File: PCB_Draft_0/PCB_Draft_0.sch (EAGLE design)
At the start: 7 parts, among them IC1 ADS7828, IC2 PCA9534PW

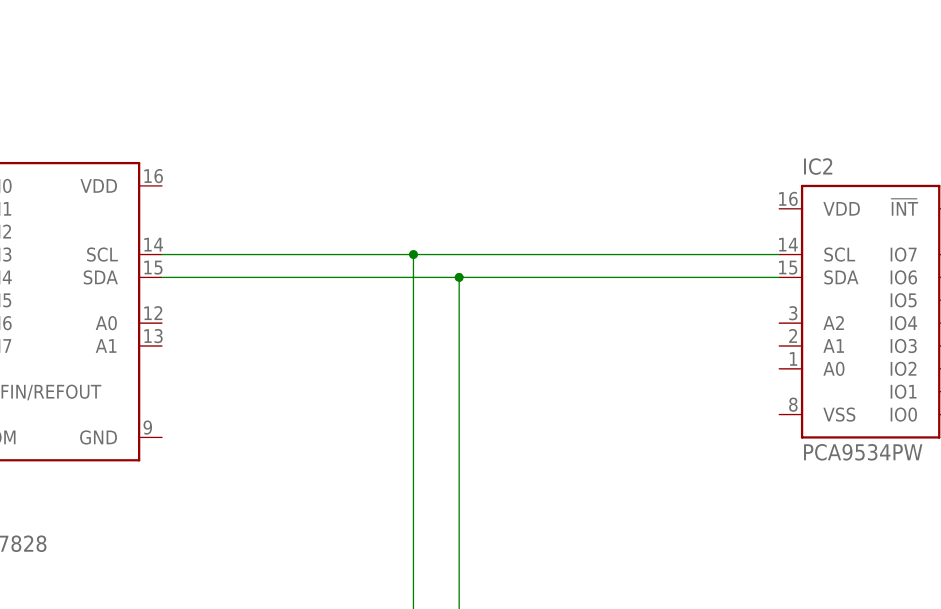
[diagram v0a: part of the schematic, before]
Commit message: With connected 3V and GND pins this time
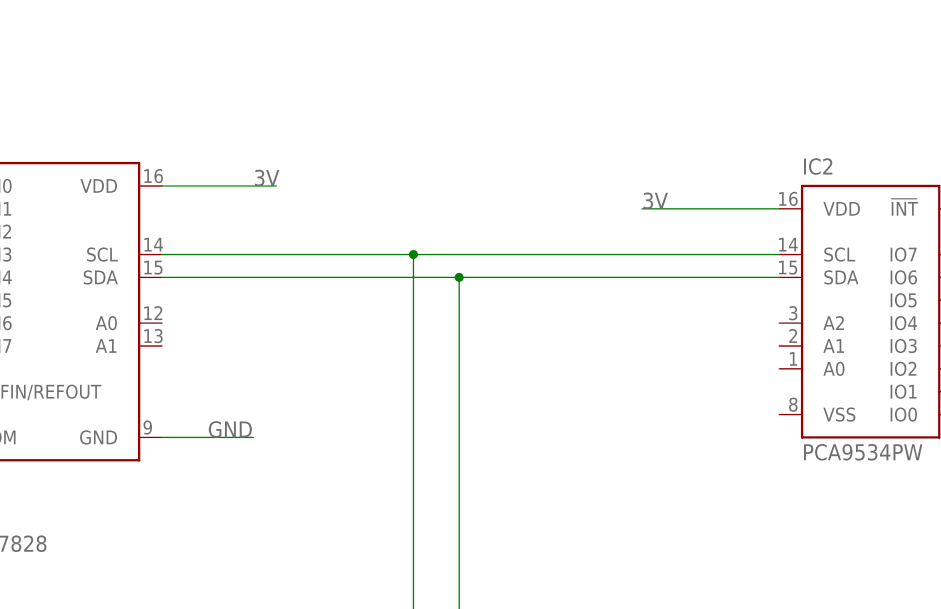
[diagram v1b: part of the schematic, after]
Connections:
- net 3V: now also IC1.VDD, IC2.VDD
- net GND: now also IC1.GND
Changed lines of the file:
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@@
 <label x="17.78" y="99.06" size="1.778" layer="95"/>
+</segment>
+<segment>
+<pinref part="IC1" gate="G$1" pin="VDD"/>
+<wire x1="104.14" y1="154.94" x2="116.84" y2="154.94" width="0.1524" layer="91"/>
+<label x="114.3" y="154.94" size="1.778" layer="95"/>
+</segment>
+<segment>
+<pinref part="IC2" gate="P" pin="VDD"/>
+<wire x1="172.72" y1="152.4" x2="157.48" y2="152.4" width="0.1524" layer="91"/>
+<label x="157.48" y="152.4" size="1.778" layer="95"/>
 </segment>
 </net>
@@
 <label x="17.78" y="91.44" size="1.778" layer="95"/>
 </segment>
+<segment>
+<pinref part="IC1" gate="G$1" pin="GND"/>
+<wire x1="104.14" y1="127" x2="114.3" y2="127" width="0.1524" layer="91"/>
+<label x="109.22" y="127" size="1.778" layer="95"/>
+</segment>
 </net>

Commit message: Added I2C Headers
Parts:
- added 3V, GND, SCL, SDA: (no value), con-lsta:FE06-1
- renumbered IC1 to ADC_X, IC2 to GPIO_X
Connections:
- net 3V: now also 3V.1, 3V.2, 3V.3, 3V.4, 3V.5, 3V.6
- net GND: now also GND.1, GND.2, GND.3, GND.4, GND.5, GND.6
- net SCL: now also SCL.1, SCL.2, SCL.3, SCL.4, SCL.5, SCL.6
- net SDA: now also SDA.1, SDA.2, SDA.3, SDA.4, SDA.5, SDA.6
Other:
- moved on the sheet: R1, R2

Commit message: SomeStuff
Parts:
- removed 3V, GND, SCL, SDA: (no value), con-lsta:FE06-1
- added A_COM: (no value), ME507:SCREWTERM_3P_254
- added C1: 5u, rcl:C-USC0805
- added I2C: (no value), con-lstb:MA04-1
- added R3: 0, rcl:R-US_M0805
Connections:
- new net A_COM: ADC_X.COM, A_COM-3.1, C1.2, R3.1
- new net INT: GPIO_X.!INT, MS1.GPIO5
- new net N$17: ADC_X.REFIN/REFOUT, C1.1
- net 3V: now also A_COM-1.1, I2C.1; no longer 3V.1, 3V.2, 3V.3, 3V.4, 3V.5, 3V.6
- net GND: now also ADC_X.A0, ADC_X.A1, A_COM-2.1, GPIO_X.A0, GPIO_X.A1, GPIO_X.A2, GPIO_X.VSS, I2C.4, R3.2; no longer GND.1, GND.2, GND.3, GND.4, GND.5, GND.6
- net SCL: now also I2C.3; no longer SCL.1, SCL.2, SCL.3, SCL.4, SCL.5, SCL.6
- net SDA: now also I2C.2; no longer SDA.1, SDA.2, SDA.3, SDA.4, SDA.5, SDA.6
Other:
- moved on the sheet: A-1, A-2, A-3, A-4, A-5, A-6, A-7, A-8, ADC_X, D-1, D-2, D-3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

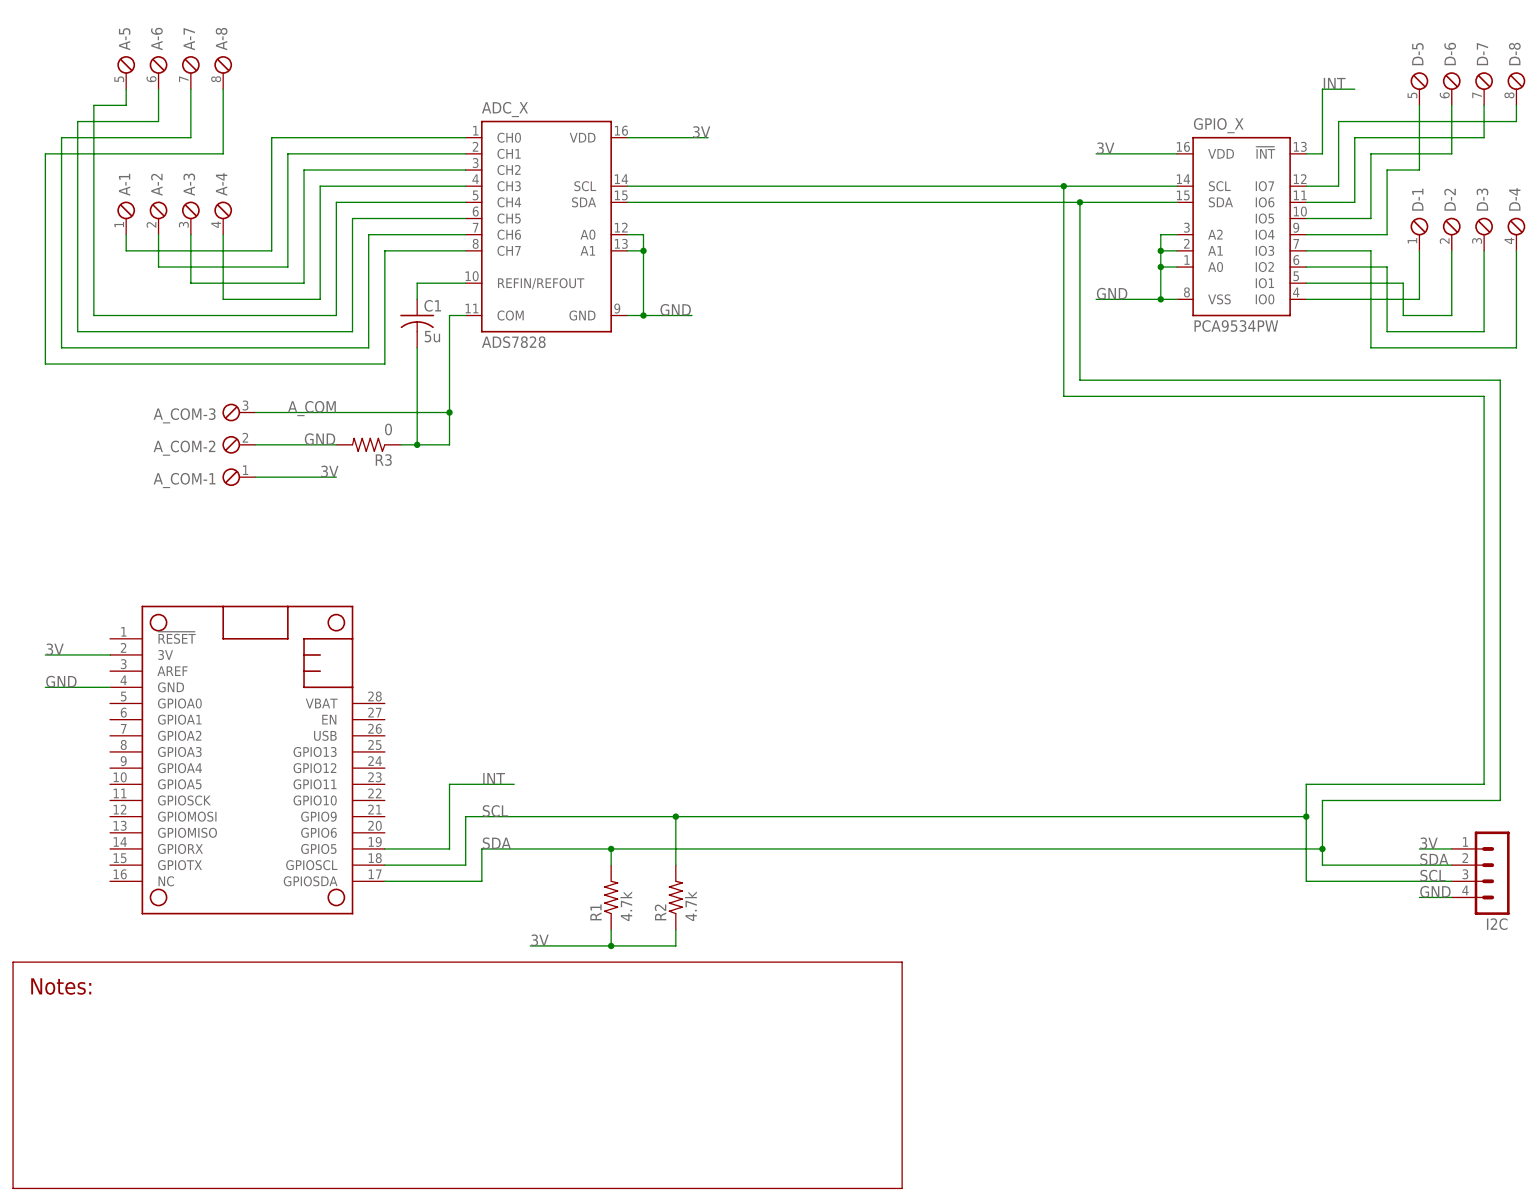
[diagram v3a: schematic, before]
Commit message: Expanded board, reorganized stuff, added motor driver
Submitted to canvas
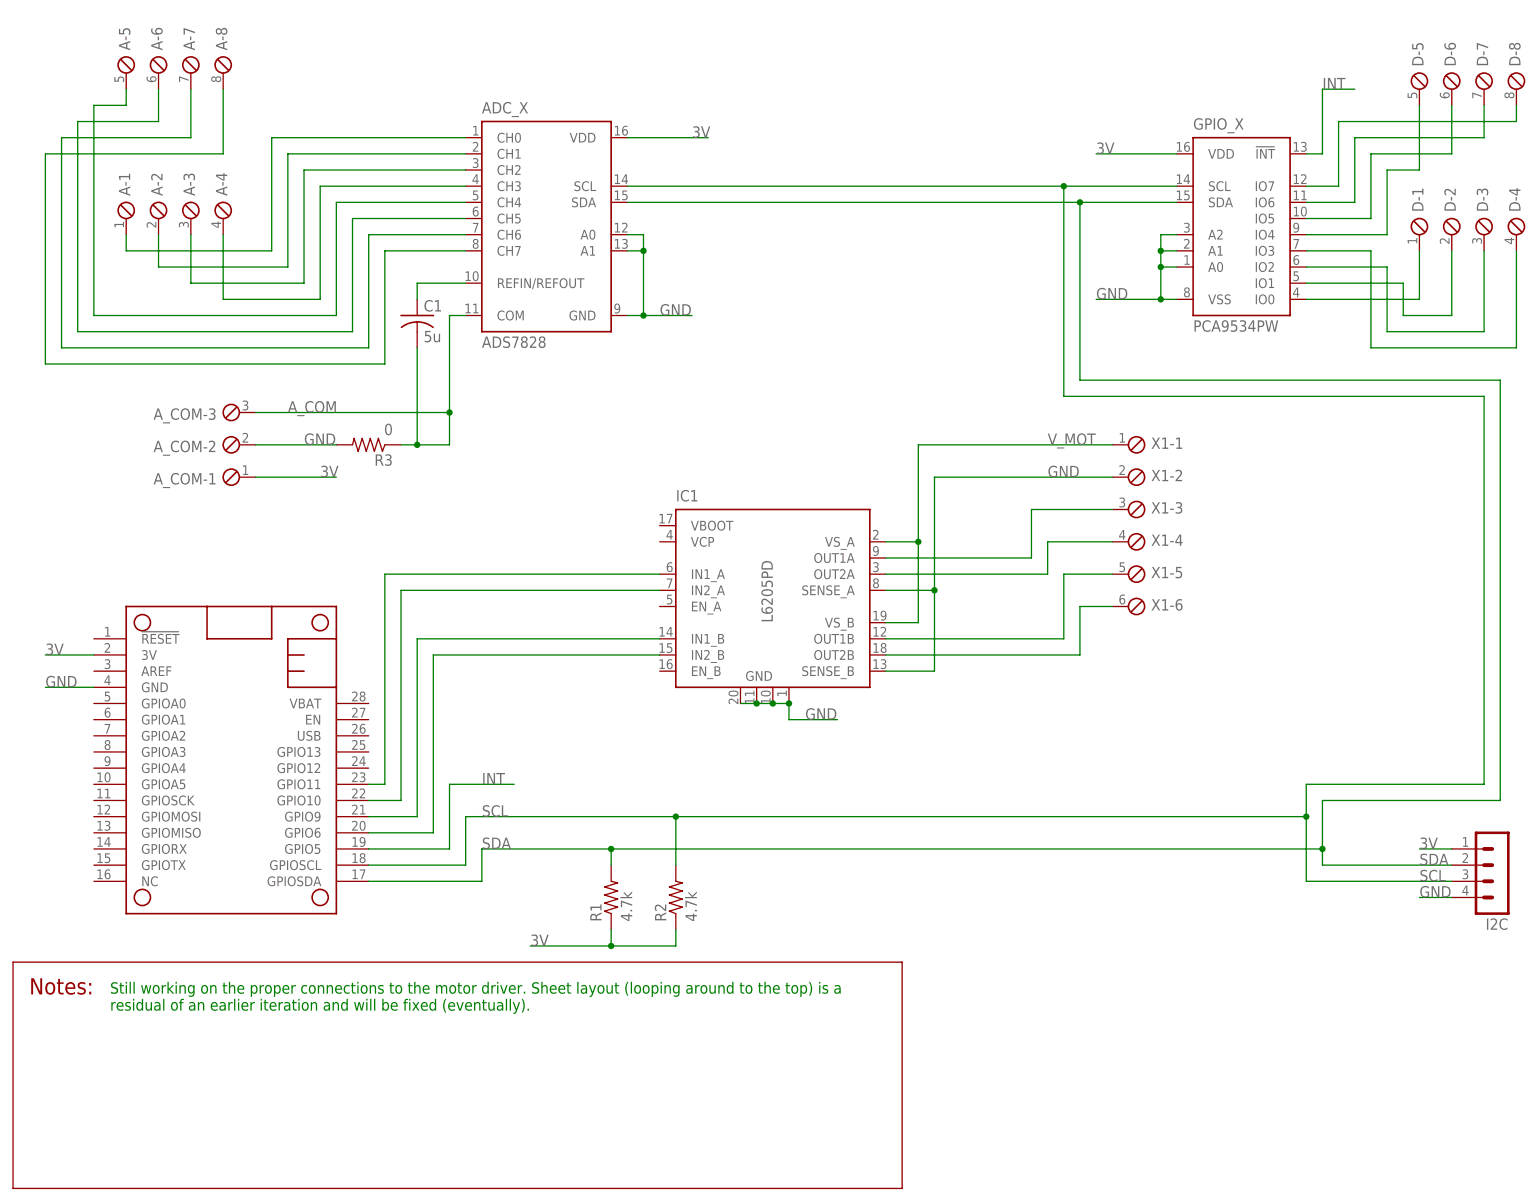
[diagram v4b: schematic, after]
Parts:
- added IC1: L6205PD, st-microelectronics:L6205PD
- added X1: (no value), ME507:SCREWTERM_6P_254
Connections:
- new net N$18: IC1.OUT1A, X1-3.1
- new net N$19: IC1.OUT2A, X1-4.1
- new net N$20: IC1.OUT1B, X1-5.1
- new net N$21: IC1.OUT2B, X1-6.1
- new net N$22: IC1.IN1_A, MS1.GPIO11
- new net N$24: IC1.IN2_B, MS1.GPIO6
- new net N$25: IC1.IN1_B, MS1.GPIO9
- new net N$26: IC1.IN2_A, MS1.GPIO10
- new net V_MOT: IC1.VS_A, IC1.VS_B, X1-1.1
- net GND: now also IC1.GND, IC1.GND@1, IC1.GND@2, IC1.GND@3, IC1.SENSE_A, IC1.SENSE_B, X1-2.1
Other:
- note added: "Still working on the proper connections to the motor driver. Sheet layout (looping around to the top) is a residual of an earlier iteration and will be fixed (eventually)."
